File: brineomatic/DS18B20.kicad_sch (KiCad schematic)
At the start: 2 parts, among them J3 THERM

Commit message: worked on bom for rev b prototype run
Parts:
- J3: value THERM -> ~
- R10: LCSC C60816 -> (none)
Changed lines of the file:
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@@
 			)
 		)
-		(property "LCSC" "C60816"
+		(property "LCSC" ""
 			(at 124.46 93.98 0)
 			(effects
@@
 			)
 		)
-		(property "Value" "THERM"
+		(property "Value" "~"
 			(at 113.03 90.17 0)
 			(effects

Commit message: updated jlc parts rotations and placement offsets
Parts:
- J3: Rotation Offset (none) -> 180
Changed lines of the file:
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@@
+			)
+		)
+		(property "Rotation Offset" "180"
+			(at 113.03 96.52 0)
+			(effects
+				(font
+					(size 1.27 1.27)
+				)
+				(hide yes)
 			)
 		)

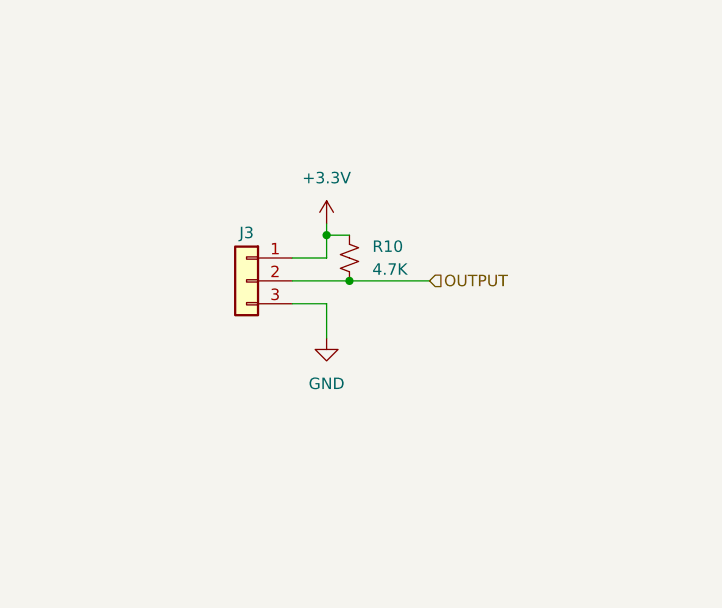
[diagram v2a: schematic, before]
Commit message: added qwiic i2c connector
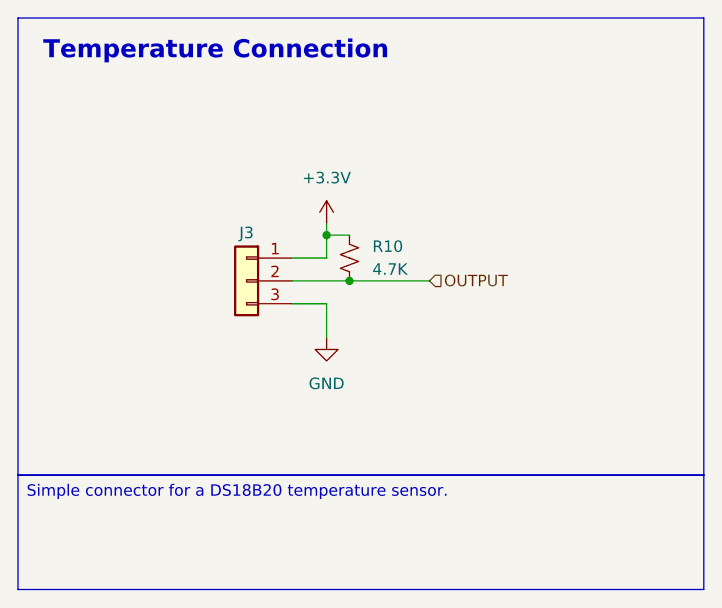
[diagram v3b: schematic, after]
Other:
- note added: "Temperature Connection"
- title: (none) -> https://github.com/hoeken/brineomatic
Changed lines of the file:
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@@
 	(generator_version "9.0")
 	(paper "A4")
+	(title_block
+		(title "https://github.com/hoeken/brineomatic")
+		(date "2025-08-28")
+		(rev "B")
+	)
+	(rectangle
+		(start 87.63 67.31)
+		(end 163.83 118.11)
+		(stroke
+			(width 0)
+			(type default)
+		)
+		(fill
+			(type none)
+		)
+	)
+	(text "Temperature Connection"
+		(exclude_from_sim no)
+		(at 90.424 70.993 0)
+		(effects
+			(font
+				(size 2 2)
+				(thickness 0.4)
+				(bold yes)
+			)
+			(justify left)
+		)
+	)
+	(text_box "Simple connector for a DS18B20 temperature sensor."
+		(exclude_from_sim no)
+		(at 87.63 118.11 0)
+		(size 76.2 12.7)
+		(margins 0.9525 0.9525 0.9525 0.9525)
+		(stroke
+			(width 0)
+			(type solid)
+		)
+		(fill
+			(type none)
+		)
+		(effects
+			(font
+				(size 1.27 1.27)
+			)
+			(justify left top)
+		)
+	)
 	(junction
 		(at 121.92 91.44)

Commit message: added pullup resistor to adc alert
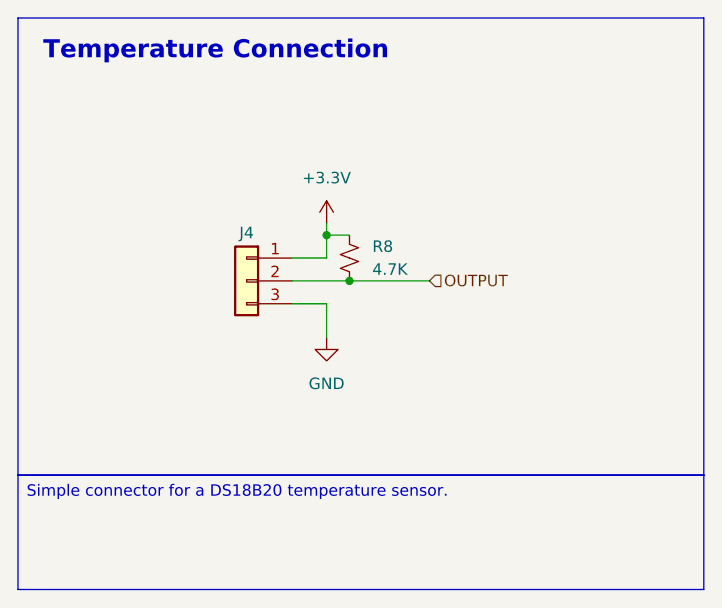
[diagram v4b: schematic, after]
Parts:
- renumbered J3 to J4, R10 to R8
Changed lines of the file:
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@@
 		(dnp no)
 		(fields_autoplaced yes)
-		(property "Reference" "#PWR014"
+		(property "Reference" "#PWR016"
 			(at 121.92 109.22 0)
 			(effects
@@
 			(project ""
 				(path "/96477ae2-ef08-48f3-8dd4-fe4478541f68/7dc38cc9-02c6-4108-8c2f-d0f758210cae"
-					(reference "#PWR014")
+					(reference "#PWR016")
 					(unit 1)
 				)
@@
 		(dnp no)
 		(fields_autoplaced yes)
-		(property "Reference" "R10"
+		(property "Reference" "R8"
 			(at 127 92.7099 0)
 			(effects
@@
 			(project "brineomatic"
 				(path "/96477ae2-ef08-48f3-8dd4-fe4478541f68/7dc38cc9-02c6-4108-8c2f-d0f758210cae"
-					(reference "R10")
+					(reference "R8")
 					(unit 1)
 				)
@@
 		(dnp no)
 		(fields_autoplaced yes)
-		(property "Reference" "#PWR013"
+		(property "Reference" "#PWR015"
 			(at 121.92 93.98 0)
 			(effects
@@
 			(project ""
 				(path "/96477ae2-ef08-48f3-8dd4-fe4478541f68/7dc38cc9-02c6-4108-8c2f-d0f758210cae"
-					(reference "#PWR013")
+					(reference "#PWR015")
 					(unit 1)
 				)
@@
 		(on_board yes)
 		(dnp no)
-		(property "Reference" "J3"
+		(property "Reference" "J4"
 			(at 113.03 91.186 0)
 			(effects
@@
 			(project ""
 				(path "/96477ae2-ef08-48f3-8dd4-fe4478541f68/7dc38cc9-02c6-4108-8c2f-d0f758210cae"
-					(reference "J3")
-					(unit 1)
-				)
+					(reference "J4")
+					(unit 1)
+				)

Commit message: added water temperature connector
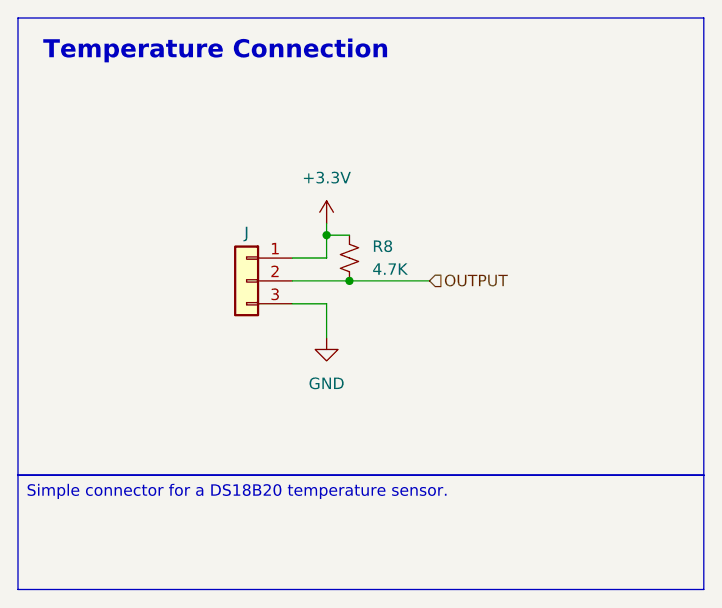
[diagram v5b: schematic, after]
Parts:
- renumbered J4 to J
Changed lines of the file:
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@@
 		(dnp no)
 		(fields_autoplaced yes)
-		(property "Reference" "#PWR016"
+		(property "Reference" "#PWR"
 			(at 121.92 109.22 0)
 			(effects
@@
 		)
 		(instances
-			(project ""
-				(path "/96477ae2-ef08-48f3-8dd4-fe4478541f68/7dc38cc9-02c6-4108-8c2f-d0f758210cae"
-					(reference "#PWR016")
+			(project "brineomatic"
+				(path "/96477ae2-ef08-48f3-8dd4-fe4478541f68/4c28a3dc-9363-4fde-b010-be952dc8ce44"
+					(reference "#PWR052")
 					(unit 1)
 				)
@@
 		(instances
 			(project "brineomatic"
+				(path "/96477ae2-ef08-48f3-8dd4-fe4478541f68/4c28a3dc-9363-4fde-b010-be952dc8ce44"
+					(reference "R?")
+					(unit 1)
+				)
 				(path "/96477ae2-ef08-48f3-8dd4-fe4478541f68/7dc38cc9-02c6-4108-8c2f-d0f758210cae"
 					(reference "R8")
@@
 		(dnp no)
 		(fields_autoplaced yes)
-		(property "Reference" "#PWR015"
+		(property "Reference" "#PWR"
 			(at 121.92 93.98 0)
 			(effects
@@
 		)
 		(instances
-			(project ""
-				(path "/96477ae2-ef08-48f3-8dd4-fe4478541f68/7dc38cc9-02c6-4108-8c2f-d0f758210cae"
-					(reference "#PWR015")
+			(project "brineomatic"
+				(path "/96477ae2-ef08-48f3-8dd4-fe4478541f68/4c28a3dc-9363-4fde-b010-be952dc8ce44"
+					(reference "#PWR051")
 					(unit 1)
 				)
@@
 		(on_board yes)
 		(dnp no)
-		(property "Reference" "J4"
+		(property "Reference" "J"
 			(at 113.03 91.186 0)
 			(effects
@@
 		)
 		(instances
-			(project ""
-				(path "/96477ae2-ef08-48f3-8dd4-fe4478541f68/7dc38cc9-02c6-4108-8c2f-d0f758210cae"
-					(reference "J4")
-					(unit 1)
-				)
+			(project "brineomatic"
+				(path "/96477ae2-ef08-48f3-8dd4-fe4478541f68/4c28a3dc-9363-4fde-b010-be952dc8ce44"
+					(reference "J?")
+					(unit 1)
+				)

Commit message: 5v power supply is sorted.
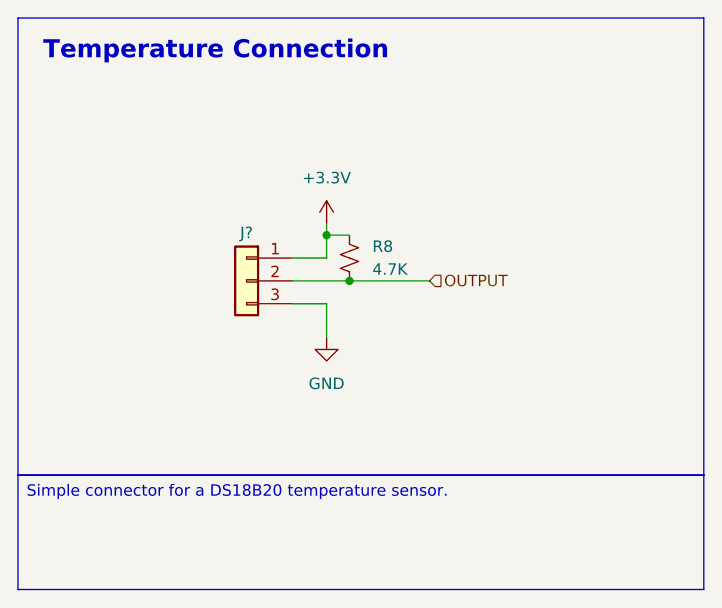
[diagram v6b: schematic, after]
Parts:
- renumbered J to J?
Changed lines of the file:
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@@
 		(dnp no)
 		(fields_autoplaced yes)
-		(property "Reference" "#PWR"
+		(property "Reference" "#PWR?"
 			(at 121.92 109.22 0)
 			(effects
@@
 				(path "/96477ae2-ef08-48f3-8dd4-fe4478541f68/4c28a3dc-9363-4fde-b010-be952dc8ce44"
 					(reference "#PWR052")
+					(unit 1)
+				)
+				(path "/96477ae2-ef08-48f3-8dd4-fe4478541f68/7dc38cc9-02c6-4108-8c2f-d0f758210cae"
+					(reference "#PWR?")
 					(unit 1)
 				)
@@
 		(dnp no)
 		(fields_autoplaced yes)
-		(property "Reference" "#PWR"
+		(property "Reference" "#PWR?"
 			(at 121.92 93.98 0)
 			(effects
@@
 				(path "/96477ae2-ef08-48f3-8dd4-fe4478541f68/4c28a3dc-9363-4fde-b010-be952dc8ce44"
 					(reference "#PWR051")
+					(unit 1)
+				)
+				(path "/96477ae2-ef08-48f3-8dd4-fe4478541f68/7dc38cc9-02c6-4108-8c2f-d0f758210cae"
+					(reference "#PWR?")
 					(unit 1)
 				)
@@
 		(on_board yes)
 		(dnp no)
-		(property "Reference" "J"
+		(property "Reference" "J?"
 			(at 113.03 91.186 0)
 			(effects
@@
 					(reference "J?")
 					(unit 1)
+				)
+				(path "/96477ae2-ef08-48f3-8dd4-fe4478541f68/7dc38cc9-02c6-4108-8c2f-d0f758210cae"
+					(reference "J?")
+					(unit 1)

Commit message: stacked tds, removed stepper vref, pulled in esp32-s3 schematic, added extra relay output
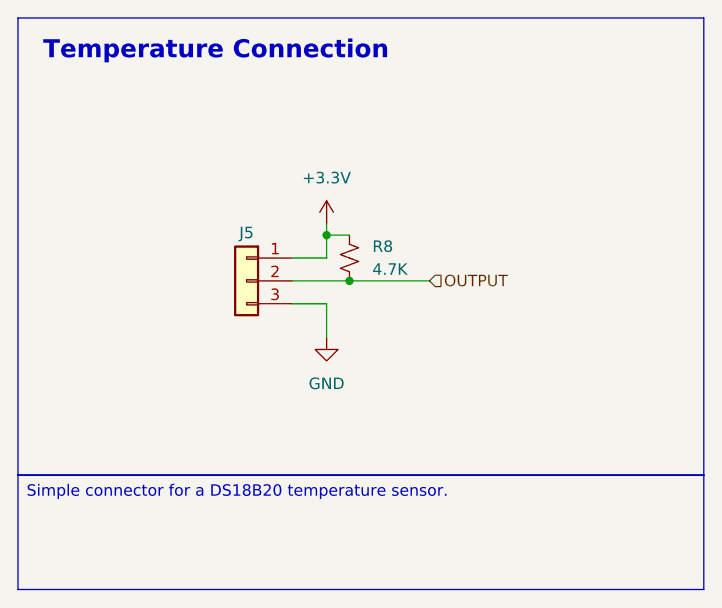
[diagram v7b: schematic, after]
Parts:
- gave numbers to parts that had none: 1
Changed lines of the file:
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@@
 		(dnp no)
 		(fields_autoplaced yes)
-		(property "Reference" "#PWR?"
+		(property "Reference" "#PWR017"
 			(at 121.92 109.22 0)
 			(effects
@@
 			(project "brineomatic"
 				(path "/96477ae2-ef08-48f3-8dd4-fe4478541f68/4c28a3dc-9363-4fde-b010-be952dc8ce44"
-					(reference "#PWR052")
-					(unit 1)
-				)
-				(path "/96477ae2-ef08-48f3-8dd4-fe4478541f68/7dc38cc9-02c6-4108-8c2f-d0f758210cae"
-					(reference "#PWR?")
+					(reference "#PWR064")
+					(unit 1)
+				)
+				(path "/96477ae2-ef08-48f3-8dd4-fe4478541f68/7dc38cc9-02c6-4108-8c2f-d0f758210cae"
+					(reference "#PWR017")
 					(unit 1)
 				)
@@
 			(project "brineomatic"
 				(path "/96477ae2-ef08-48f3-8dd4-fe4478541f68/4c28a3dc-9363-4fde-b010-be952dc8ce44"
-					(reference "R?")
+					(reference "R46")
 					(unit 1)
 				)
@@
 		(dnp no)
 		(fields_autoplaced yes)
-		(property "Reference" "#PWR?"
+		(property "Reference" "#PWR016"
 			(at 121.92 93.98 0)
 			(effects
@@
 			(project "brineomatic"
 				(path "/96477ae2-ef08-48f3-8dd4-fe4478541f68/4c28a3dc-9363-4fde-b010-be952dc8ce44"
-					(reference "#PWR051")
-					(unit 1)
-				)
-				(path "/96477ae2-ef08-48f3-8dd4-fe4478541f68/7dc38cc9-02c6-4108-8c2f-d0f758210cae"
-					(reference "#PWR?")
+					(reference "#PWR063")
+					(unit 1)
+				)
+				(path "/96477ae2-ef08-48f3-8dd4-fe4478541f68/7dc38cc9-02c6-4108-8c2f-d0f758210cae"
+					(reference "#PWR016")
 					(unit 1)
 				)
@@
 		(on_board yes)
 		(dnp no)
-		(property "Reference" "J?"
+		(property "Reference" "J5"
 			(at 113.03 91.186 0)
 			(effects
@@
 			(project "brineomatic"
 				(path "/96477ae2-ef08-48f3-8dd4-fe4478541f68/4c28a3dc-9363-4fde-b010-be952dc8ce44"
-					(reference "J?")
-					(unit 1)
-				)
-				(path "/96477ae2-ef08-48f3-8dd4-fe4478541f68/7dc38cc9-02c6-4108-8c2f-d0f758210cae"
-					(reference "J?")
-					(unit 1)
-				)
+					(reference "J21")
+					(unit 1)
+				)
+				(path "/96477ae2-ef08-48f3-8dd4-fe4478541f68/7dc38cc9-02c6-4108-8c2f-d0f758210cae"
+					(reference "J5")
+					(unit 1)
+				)
